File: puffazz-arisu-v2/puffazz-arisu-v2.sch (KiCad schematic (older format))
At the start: 185 parts, among them SW1 SW_Push, U1 ATmega32U4-AU, Y1 16MHz

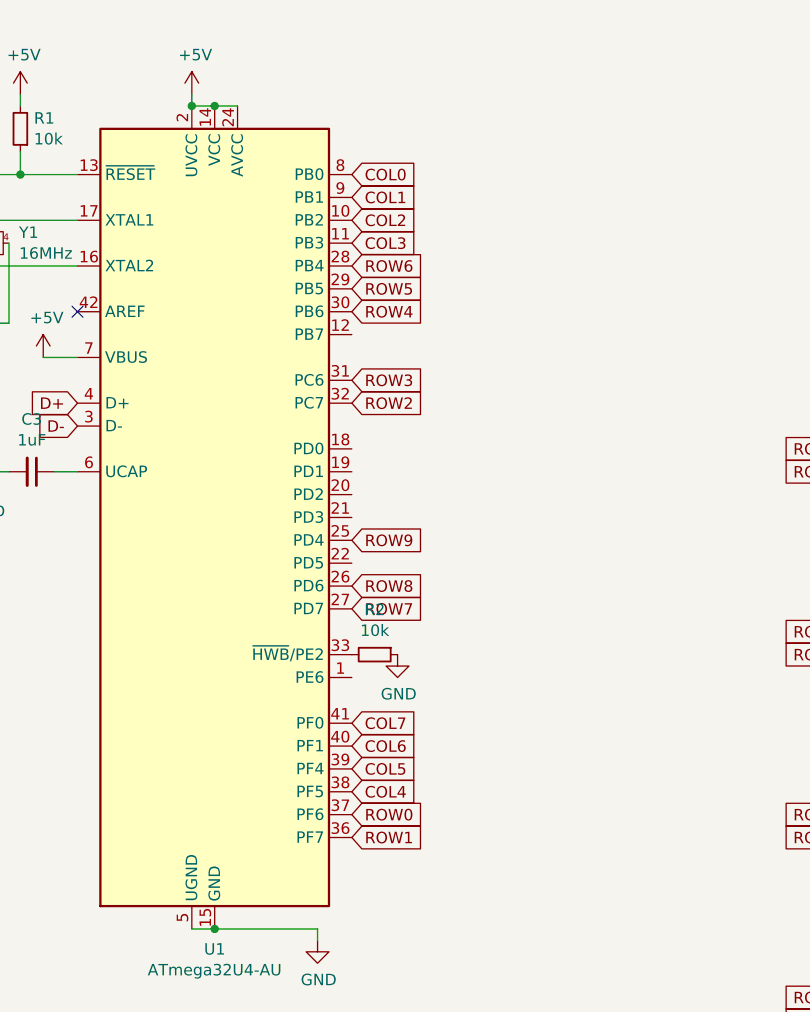
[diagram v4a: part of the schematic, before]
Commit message: Completed placing all components, missing some 5V routes.
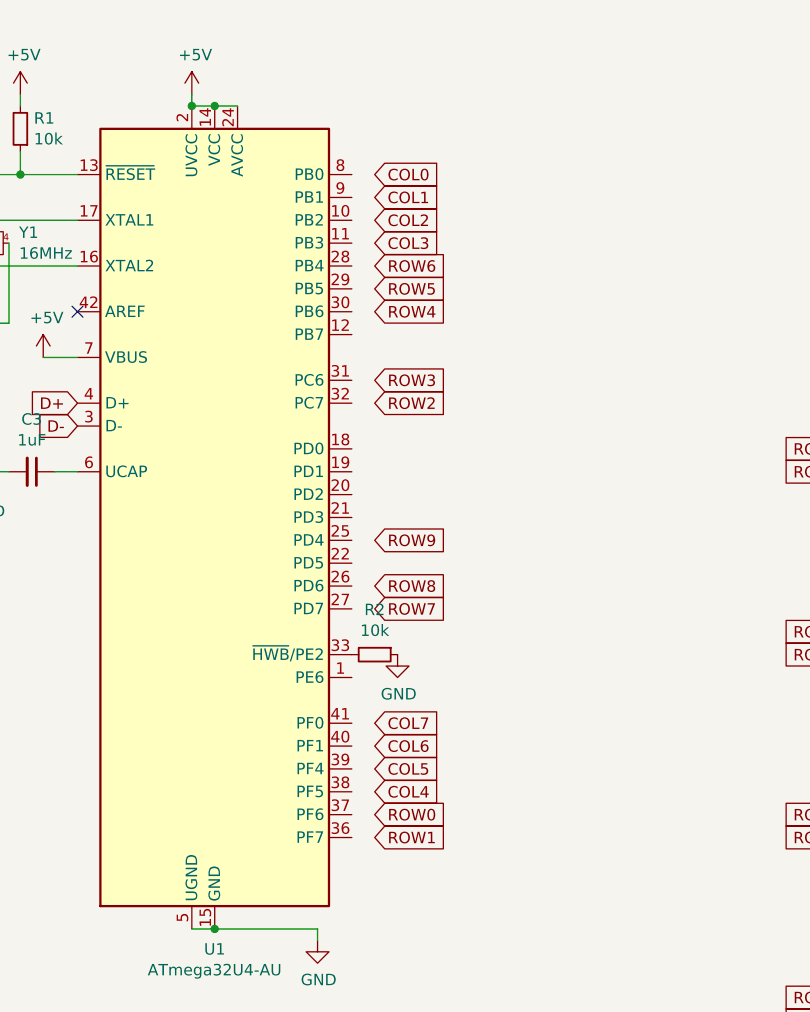
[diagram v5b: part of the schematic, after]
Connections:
- net COL0: no longer U1.8 (PB0)
- net COL1: no longer U1.9 (PB1)
- net COL2: no longer U1.10 (PB2)
- net COL3: no longer U1.11 (PB3)
- net COL4: no longer U1.38 (PF5)
- net COL5: no longer U1.39 (PF4)
- net COL6: no longer U1.40 (PF1)
- net COL7: no longer U1.41 (PF0)
- net ROW0: no longer U1.37 (PF6)
- net ROW1: no longer U1.36 (PF7)
- net ROW2: no longer U1.32 (PC7)
- net ROW3: no longer U1.31 (PC6)
- net ROW4: no longer U1.30 (PB6)
- net ROW5: no longer U1.29 (PB5)
- net ROW6: no longer U1.28 (PB4)
- net ROW7: no longer U1.27 (PD7)
- net ROW8: no longer U1.26 (PD6)
- net ROW9: no longer U1.25 (PD4)
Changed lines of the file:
@@
 	1    0    0    -1
 $EndComp
-Text GLabel 3500 1350 2    50   Input ~ 0
+Text GLabel 3600 1350 2    50   Input ~ 0
 COL0
-Text GLabel 3500 1450 2    50   Input ~ 0
+Text GLabel 3600 1450 2    50   Input ~ 0
 COL1
-Text GLabel 3500 1550 2    50   Input ~ 0
+Text GLabel 3600 1550 2    50   Input ~ 0
 COL2
-Text GLabel 3500 1650 2    50   Input ~ 0
+Text GLabel 3600 1650 2    50   Input ~ 0
 COL3
-Text GLabel 3500 3750 2    50   Input ~ 0
+Text GLabel 3600 3750 2    50   Input ~ 0
 COL7
-Text GLabel 3500 3850 2    50   Input ~ 0
+Text GLabel 3600 3850 2    50   Input ~ 0
 COL6
-Text GLabel 3500 3950 2    50   Input ~ 0
+Text GLabel 3600 3950 2    50   Input ~ 0
 COL5
-Text GLabel 3500 4050 2    50   Input ~ 0
+Text GLabel 3600 4050 2    50   Input ~ 0
 COL4
-Text GLabel 3500 4150 2    50   Input ~ 0
+Text GLabel 3600 4150 2    50   Input ~ 0
 ROW0
-Text GLabel 3500 4250 2    50   Input ~ 0
+Text GLabel 3600 4250 2    50   Input ~ 0
 ROW1
-Text GLabel 3500 2350 2    50   Input ~ 0
+Text GLabel 3600 2350 2    50   Input ~ 0
 ROW2
-Text GLabel 3500 2250 2    50   Input ~ 0
+Text GLabel 3600 2250 2    50   Input ~ 0
 ROW3
-Text GLabel 3500 1950 2    50   Input ~ 0
+Text GLabel 3600 1950 2    50   Input ~ 0
 ROW4
-Text GLabel 3500 1850 2    50   Input ~ 0
+Text GLabel 3600 1850 2    50   Input ~ 0
 ROW5
-Text GLabel 3500 1750 2    50   Input ~ 0
+Text GLabel 3600 1750 2    50   Input ~ 0
 ROW6
-Text GLabel 3500 3250 2    50   Input ~ 0
+Text GLabel 3600 3250 2    50   Input ~ 0
 ROW7
-Text GLabel 3500 3150 2    50   Input ~ 0
+Text GLabel 3600 3150 2    50   Input ~ 0
 ROW8
-Text GLabel 3500 2950 2    50   Input ~ 0
+Text GLabel 3600 2950 2    50   Input ~ 0
 ROW9
 Wire Wire Line

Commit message: Finished routing all the components
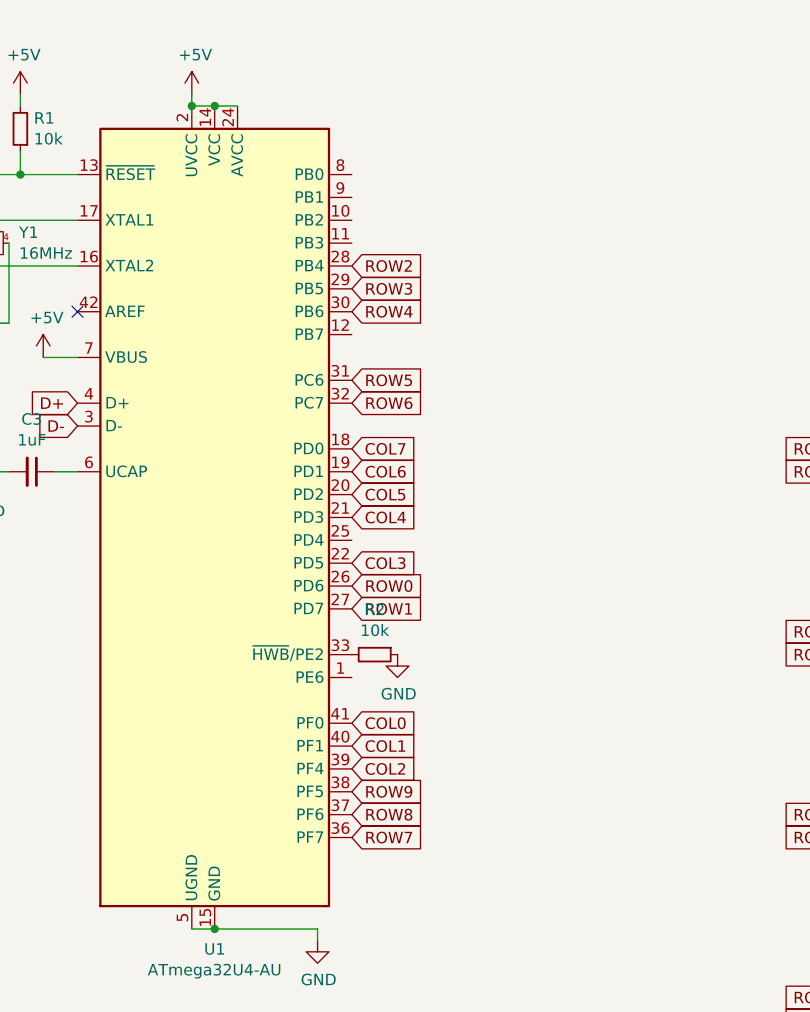
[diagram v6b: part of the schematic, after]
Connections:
- net COL0: now also U1.41 (PF0)
- net COL1: now also U1.40 (PF1)
- net COL2: now also U1.39 (PF4)
- net COL3: now also U1.22 (PD5)
- net COL4: now also U1.21 (PD3)
- net COL5: now also U1.20 (PD2)
- net COL6: now also U1.19 (PD1)
- net COL7: now also U1.18 (PD0)
- net ROW0: now also U1.26 (PD6)
- net ROW1: now also U1.27 (PD7)
- net ROW2: now also U1.28 (PB4)
- net ROW3: now also U1.29 (PB5)
- net ROW4: now also U1.30 (PB6)
- net ROW5: now also U1.31 (PC6)
- net ROW6: now also U1.32 (PC7)
- net ROW7: now also U1.36 (PF7)
- net ROW8: now also U1.37 (PF6)
- net ROW9: now also U1.38 (PF5)
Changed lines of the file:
@@
 	1    0    0    -1
 $EndComp
-Text GLabel 3600 1350 2    50   Input ~ 0
+Text GLabel 3500 3750 2    50   Input ~ 0
 COL0
-Text GLabel 3600 1450 2    50   Input ~ 0
+Text GLabel 3500 3850 2    50   Input ~ 0
 COL1
-Text GLabel 3600 1550 2    50   Input ~ 0
+Text GLabel 3500 3950 2    50   Input ~ 0
 COL2
-Text GLabel 3600 1650 2    50   Input ~ 0
+Text GLabel 3500 3050 2    50   Input ~ 0
 COL3
-Text GLabel 3600 3750 2    50   Input ~ 0
+Text GLabel 3500 2550 2    50   Input ~ 0
 COL7
-Text GLabel 3600 3850 2    50   Input ~ 0
+Text GLabel 3500 2650 2    50   Input ~ 0
 COL6
-Text GLabel 3600 3950 2    50   Input ~ 0
+Text GLabel 3500 2750 2    50   Input ~ 0
 COL5
-Text GLabel 3600 4050 2    50   Input ~ 0
+Text GLabel 3500 2850 2    50   Input ~ 0
 COL4
-Text GLabel 3600 4150 2    50   Input ~ 0
+Text GLabel 3500 3150 2    50   Input ~ 0
 ROW0
-Text GLabel 3600 4250 2    50   Input ~ 0
+Text GLabel 3500 3250 2    50   Input ~ 0
 ROW1
-Text GLabel 3600 2350 2    50   Input ~ 0
+Text GLabel 3500 1750 2    50   Input ~ 0
 ROW2
-Text GLabel 3600 2250 2    50   Input ~ 0
+Text GLabel 3500 1850 2    50   Input ~ 0
 ROW3
-Text GLabel 3600 1950 2    50   Input ~ 0
+Text GLabel 3500 1950 2    50   Input ~ 0
 ROW4
-Text GLabel 3600 1850 2    50   Input ~ 0
+Text GLabel 3500 2250 2    50   Input ~ 0
 ROW5
-Text GLabel 3600 1750 2    50   Input ~ 0
+Text GLabel 3500 2350 2    50   Input ~ 0
 ROW6
-Text GLabel 3600 3250 2    50   Input ~ 0
+Text GLabel 3500 4250 2    50   Input ~ 0
 ROW7
-Text GLabel 3600 3150 2    50   Input ~ 0
+Text GLabel 3500 4150 2    50   Input ~ 0
 ROW8
-Text GLabel 3600 2950 2    50   Input ~ 0
+Text GLabel 3500 4050 2    50   Input ~ 0
 ROW9
 Wire Wire Line

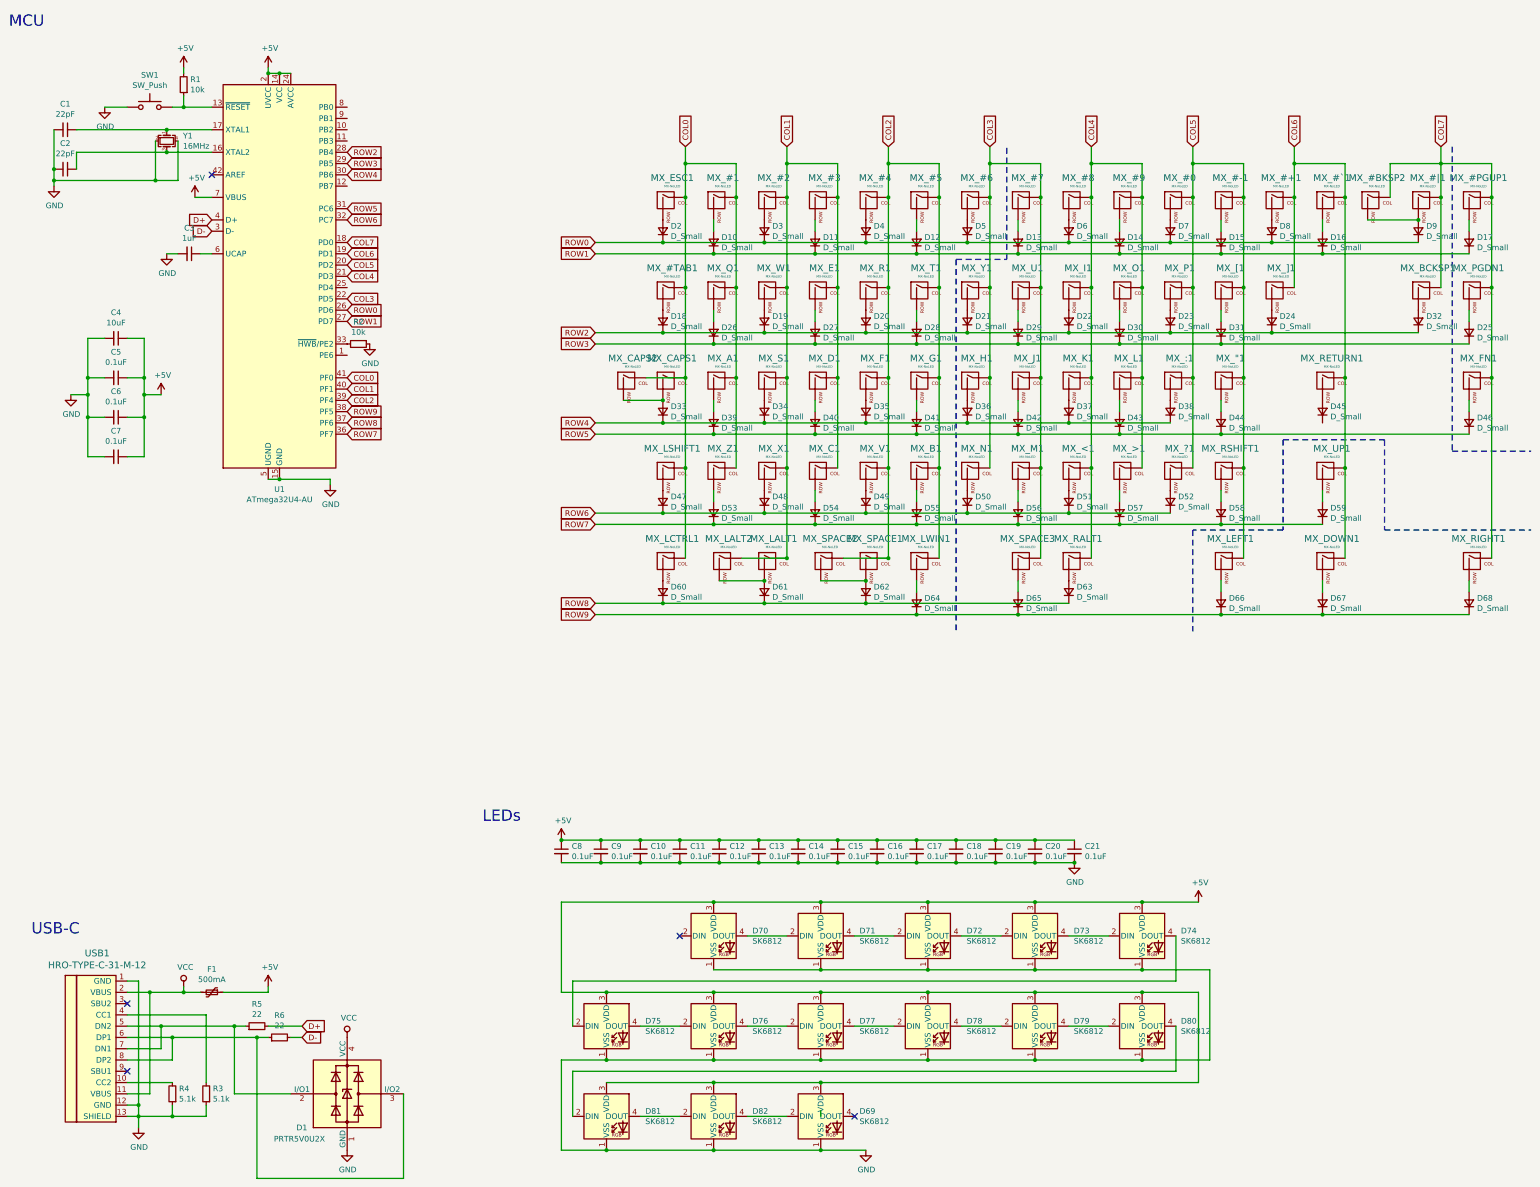
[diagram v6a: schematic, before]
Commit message: Tidied up underglow RGB traces
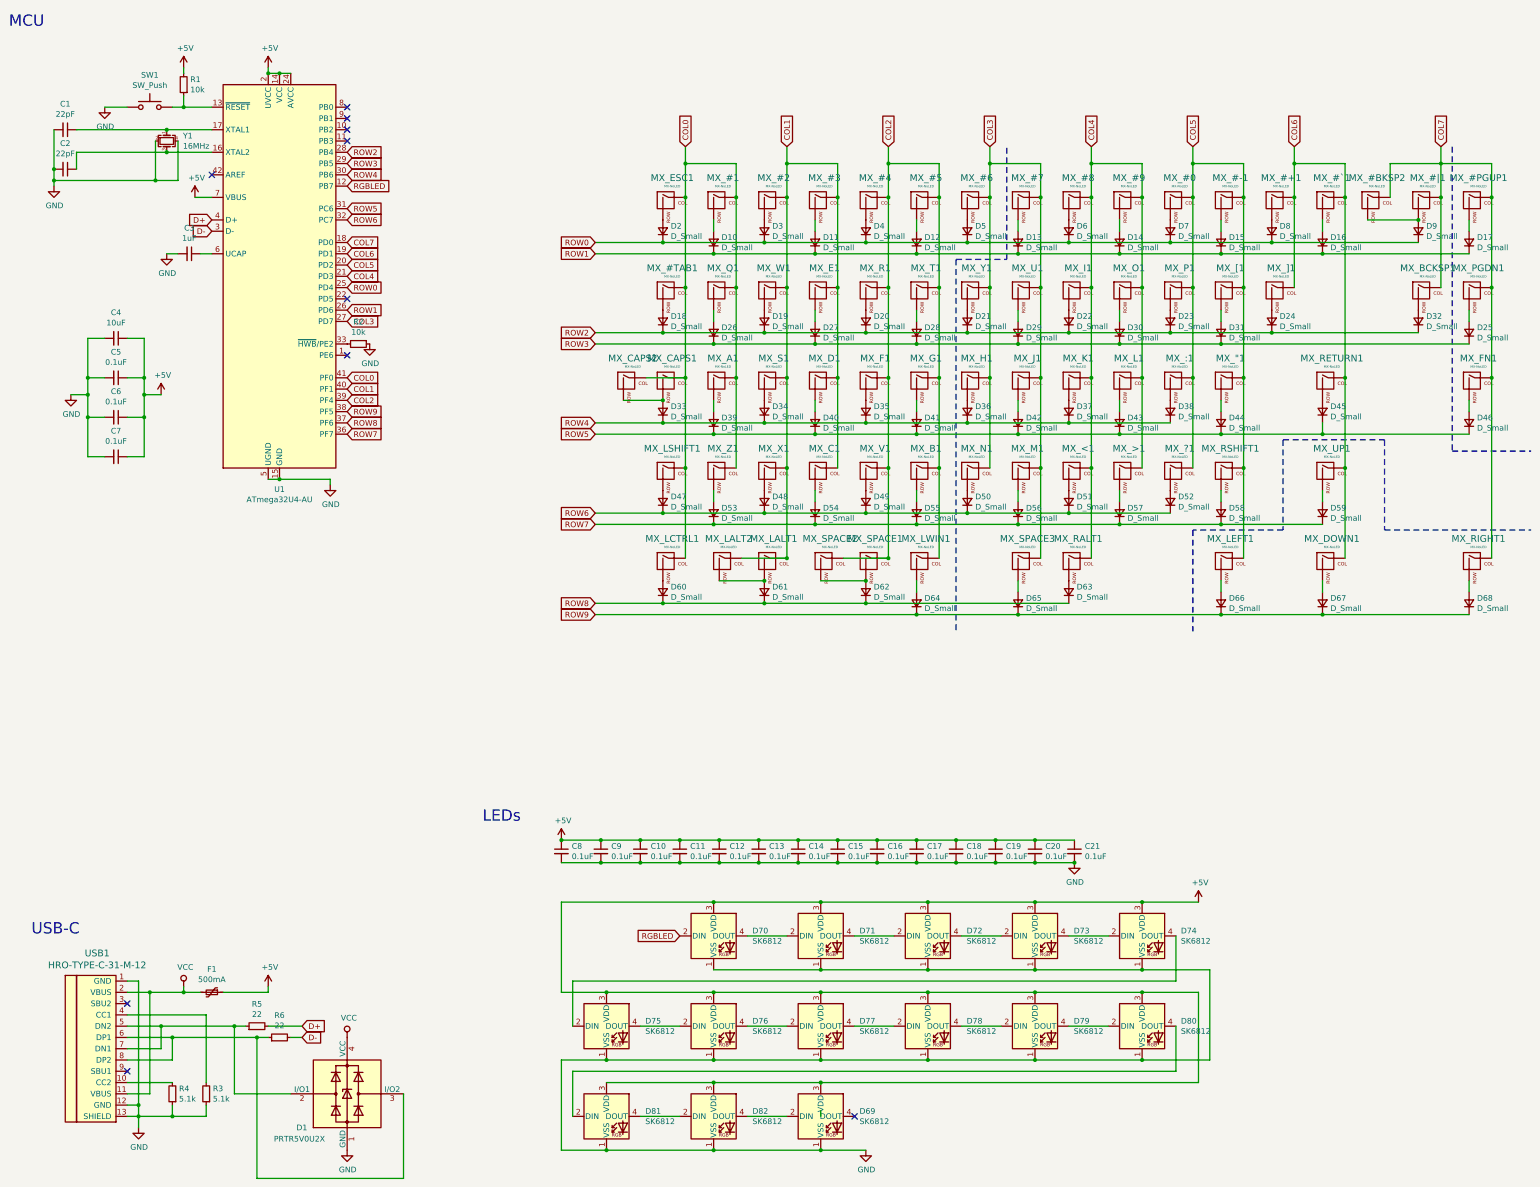
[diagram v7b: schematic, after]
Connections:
- net COL3: now also U1.27 (PD7); no longer U1.22 (PD5)
- net ROW0: now also U1.25 (PD4); no longer U1.26 (PD6)
- net ROW1: now also U1.26 (PD6); no longer U1.27 (PD7)
- net ROW5: now also D45.1 (K)
- net RGBLED: now reaches U1.12 (PB7)
- net RGBLED: now also D70.2 (DIN)
- no-connect marks 5 -> 10
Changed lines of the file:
@@
 Text GLabel 3500 3950 2    50   Input ~ 0
 COL2
-Text GLabel 3500 3050 2    50   Input ~ 0
+Text GLabel 3500 3250 2    50   Input ~ 0
 COL3
 Text GLabel 3500 2550 2    50   Input ~ 0
@@
 Text GLabel 3500 2850 2    50   Input ~ 0
 COL4
+Text GLabel 3500 2950 2    50   Input ~ 0
+ROW0
 Text GLabel 3500 3150 2    50   Input ~ 0
-ROW0
-Text GLabel 3500 3250 2    50   Input ~ 0
 ROW1
 Text GLabel 3500 1750 2    50   Input ~ 0
@@
 $EndComp
 Wire Wire Line
-	11250 4250 13450 4250
+	11250 4250 12150 4250
 Wire Wire Line
 	7700 10300 7700 10250
@@
 	7400 10300 7050 10300
 NoConn ~ 8000 10300
-NoConn ~ 6450 8700
+Wire Wire Line
+	12150 4150 12150 4250
+Connection ~ 12150 4250
+Wire Wire Line
+	12150 4250 13450 4250
+Text GLabel 6450 8700 0    50   Input ~ 0
+RGBLED
+Text GLabel 3500 2050 2    50   Input ~ 0
+RGBLED
+NoConn ~ 3500 1350
+NoConn ~ 3500 1450
+NoConn ~ 3500 1550
+NoConn ~ 3500 1650
+NoConn ~ 3500 3050
+NoConn ~ 3500 3550
 $EndSCHEMATC
